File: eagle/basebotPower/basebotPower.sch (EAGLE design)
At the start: 7 parts

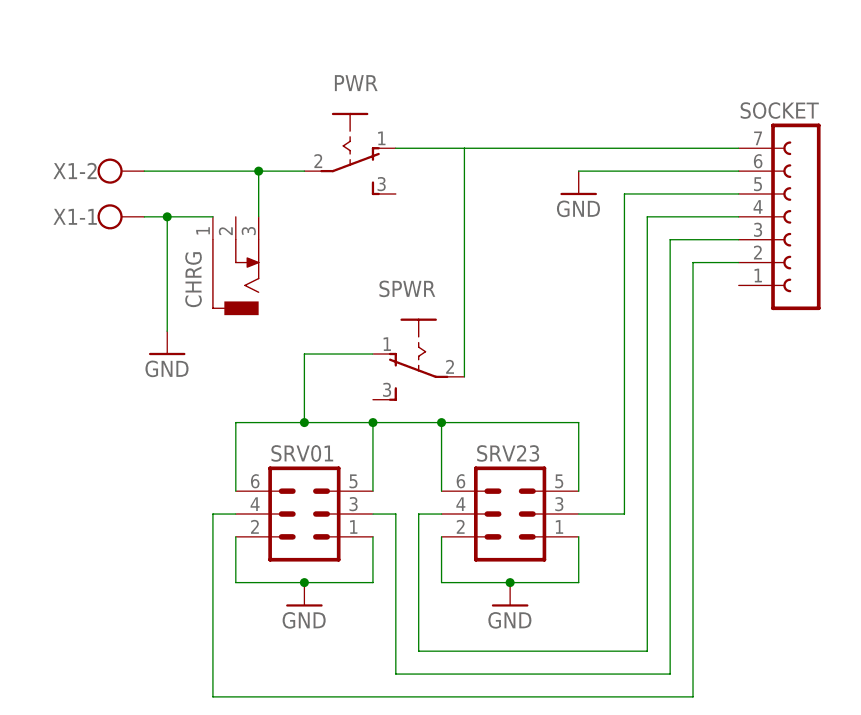
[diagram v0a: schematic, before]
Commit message: Fixed stupid error in board involving the wrong wiring for the servos, also changed the layout to use screw terminals rather than on board switches, this allows for panel mount (and higher current) switches and means the board itself can be tucked away somewhere.
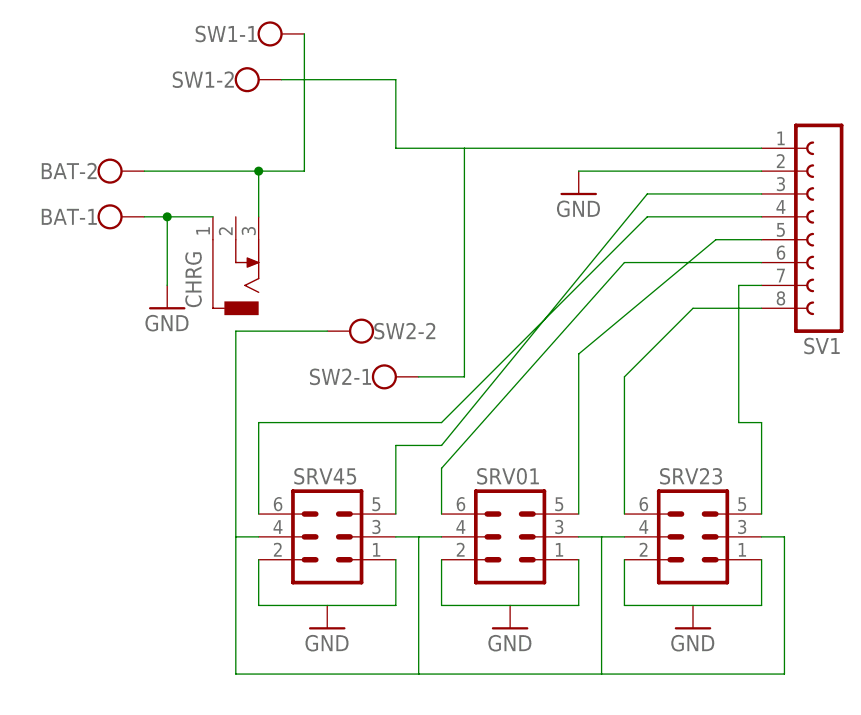
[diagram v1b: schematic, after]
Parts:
- removed PWR, SPWR: (no value), switch:255SB
- removed SOCKET: (no value), con-lsta:FE07-1
- added SRV45: (no value), con-lstb:MA03-2
- added SV1: (no value), con-lsta:FE08-1
- added SW1, SW2: (no value), con-wago-500:W237-102
- renumbered X1 to BAT
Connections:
- new net N$12: SRV01.3, SRV01.4, SRV23.3, SRV23.4, SRV45.3, SRV45.4, SW2-2.KL
- new net N$4: SRV23.5, SV1.7
- net GND: now also SRV45.1, SRV45.2, SV1.2; no longer SOCKET.6
- net N$2: now also SW1-1.KL; no longer PWR.P
- net N$3: now also SV1.8; no longer SPWR.O, SRV01.5, SRV01.6, SRV23.5
- net N$5: now also SRV45.6, SV1.4; no longer SOCKET.5, SRV23.3
- net N$6: now also SRV45.5, SV1.3; no longer SOCKET.4, SRV23.4
- net N$7: now also SRV01.6, SV1.6; no longer SOCKET.3, SRV01.3
- net N$9: now also SRV01.5, SV1.5; no longer SOCKET.2, SRV01.4
- net SERVOPWR: now also SV1.1, SW1-2.KL, SW2-1.KL; no longer PWR.O, SOCKET.7, SPWR.P
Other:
- moved on the sheet: SRV01, SRV23
